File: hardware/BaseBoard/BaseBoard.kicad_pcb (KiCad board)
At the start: 2 copper layers, 81.3 x 106.7 mm, 83 parts, among them J1 I2C, J1-ESP1 ESP-1-L, J1-ESP2 ESP-1-L, J1-ESP3 ESP-1-L, J1-ESP4 ESP-1-L, J1-ESP5 ESP-1-L, J1-ESP6 ESP-1-L, J1-ESP7 ESP-1-L, J1-ESP8 ESP-1-L, J2 3V3P0_7, J2-ESP1 ESP-1-R, J2-ESP2 ESP-1-R, J2-ESP3 ESP-1-R, J2-ESP4 ESP-1-R, J2-ESP5 ESP-1-R, J2-ESP6 ESP-1-R, J2-ESP7 ESP-1-R, J2-ESP8 ESP-1-R, J3-BUS1 BUS-IN, J3-BUS2 BUS-IN, J3-BUS3 BUS-IN, J3-BUS4 BUS-IN, J3-BUS5 BUS-IN, J3-BUS6 BUS-IN, J3-BUS7 BUS-IN, J3-BUS8 BUS-IN, J4-BUS1 BUS-OUT, J4-BUS2 BUS-OUT, J4-BUS3 BUS-OUT, J4-BUS4 BUS-OUT, J4-BUS5 BUS-OUT, J4-BUS6 BUS-OUT, J4-BUS7 BUS-OUT, J4-BUS8 BUS-OUT, Q11 2N3904, Q12 AO3401A, Q21 2N3904, Q22 AO3401A, Q31 2N3904, Q32 AO3401A, Q41 2N3904, Q42 AO3401A, Q51 2N3904, Q52 AO3401A, Q61 2N3904, Q62 AO3401A, Q71 2N3904, Q72 AO3401A, Q81 2N3904, Q82 AO3401A, U1 AMS1117-3.3

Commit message: BaseBoard v1.1 update.
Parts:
- removed J1: I2C, Connector_PinSocket_2.54mm:PinSocket_1x04_P2.54mm_Vertical
- removed J2: 3V3P0_7, Connector_PinSocket_2.54mm:PinSocket_1x09_P2.54mm_Vertical
- added IC1: PCF8574RGTR, LIB_PCF8574RGTR:QFN50P300X300X100-17N-D, F.Cu at (179.4, 68.5)
- added R1: 10k, Resistor_SMD:R_0201_0603Metric, F.Cu at (180.6, 72.1)
- added R2: 10k, Resistor_SMD:R_0201_0603Metric, F.Cu at (181.9, 72.1)
- added R3: 10k, Resistor_SMD:R_0201_0603Metric, F.Cu at (179.3, 72.1)
- added R4: 10k, Resistor_SMD:R_0201_0603Metric, F.Cu at (181.2, 65.7)
- added R5: 10k, Resistor_SMD:R_0201_0603Metric, F.Cu at (182.2, 65.7)
- added R6: 10k, Resistor_SMD:R_0201_0603Metric, F.Cu at (183.3, 65.7)
- added SW1: SW_DIP_SPSTx03, Button_Switch_SMD:SW_DIP_SPSTx03_Slide_6.7x9.18mm_W8.61mm_P2.54mm_LowProfile, F.Cu at (189.5, 69.8)
- C1, C2: footprint Capacitor_THT:CP_Radial_D6.3mm_P2.50mm -> Capacitor_SMD:CP_Elec_4x5.3
- R11, R12, R21, R22, R31, R32, R41, R42, R51, R52, R61, R62, R71, R72, R81, R82: footprint Resistor_THT:R_Axial_DIN0207_L6.3mm_D2.5mm_P7.62mm_Horizontal -> Resistor_SMD:R_0603_1608Metric
- moved R22 12.0 mm to (177.8, 100.6), turned to -90 degrees
- moved R12 12.0 mm to (198.1, 100.6), turned to -90 degrees
- moved R32 12.0 mm to (157.5, 100.6), turned to -90 degrees
- moved R42 12.0 mm to (137.2, 100.6), turned to -90 degrees
- moved R62 11.5 mm to (147.3, 43.7), turned to 90 degrees
- moved R72 11.5 mm to (167.6, 43.7), turned to 90 degrees
- moved R52 11.5 mm to (127.0, 43.7), turned to 90 degrees
- moved R82 11.5 mm to (188.0, 43.7), turned to 90 degrees
- moved R51 9.74 mm to (133.3, 45.0), turned to 180 degrees
- moved R61 9.74 mm to (153.7, 45.0), turned to 180 degrees
- moved R81 9.74 mm to (194.3, 45.0), turned to 180 degrees
- moved R71 9.74 mm to (174.0, 45.0), turned to 180 degrees
- moved R11 9.23 mm to (191.8, 99.3), turned to 0 degrees
- moved R41 9.23 mm to (130.8, 99.3), turned to 0 degrees
- moved R21 9.23 mm to (171.4, 99.3), turned to 0 degrees
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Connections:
- net Net-(J1-Pin_1) renamed +3V3
- J1-ESP1 pad 6: unconnected-(J1-ESP1-Pin_6-Pad6) -> Net-(J1-ESP1-Pin_6)
- J1-ESP2 pad 6: unconnected-(J1-ESP2-Pin_6-Pad6) -> Net-(J1-ESP2-Pin_6)
- J1-ESP3 pad 6: unconnected-(J1-ESP3-Pin_6-Pad6) -> Net-(J1-ESP3-Pin_6)
- J1-ESP4 pad 6: unconnected-(J1-ESP4-Pin_6-Pad6) -> Net-(J1-ESP4-Pin_6)
- J1-ESP5 pad 6: unconnected-(J1-ESP5-Pin_6-Pad6) -> Net-(J1-ESP5-Pin_6)
- J1-ESP6 pad 6: unconnected-(J1-ESP6-Pin_6-Pad6) -> Net-(J1-ESP6-Pin_6)
- J1-ESP7 pad 6: unconnected-(J1-ESP7-Pin_6-Pad6) -> Net-(J1-ESP7-Pin_6)
- J1-ESP8 pad 6: unconnected-(J1-ESP8-Pin_6-Pad6) -> Net-(J1-ESP8-Pin_6)
- J3-BUS1 pad 2: GNDREF -> Net-(J1-ESP1-Pin_6)
- J3-BUS2 pad 2: GNDREF -> Net-(J1-ESP2-Pin_6)
- J3-BUS3 pad 2: GNDREF -> Net-(J1-ESP3-Pin_6)
- J3-BUS4 pad 2: GNDREF -> Net-(J1-ESP4-Pin_6)
- J3-BUS5 pad 2: GNDREF -> Net-(J1-ESP5-Pin_6)
- J3-BUS6 pad 2: GNDREF -> Net-(J1-ESP6-Pin_6)
- J3-BUS7 pad 2: GNDREF -> Net-(J1-ESP7-Pin_6)
- J3-BUS8 pad 2: GNDREF -> Net-(J1-ESP8-Pin_6)
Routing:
- net SWPIN-ESP4: track 24.9 -> 72.8 mm, vias 0 -> 2
- net SWPIN-ESP3: track 6.66 -> 52.4 mm, vias 0 -> 2
- net SWPIN-ESP5: track 25.4 -> 67.9 mm, vias 0 -> 2
- net SWPIN-ESP8: track 66.9 -> 34.6 mm, vias 0 -> 2
- net SWPIN-ESP2: track 14.3 -> 38.7 mm, vias 0 -> 2
- net SWPIN-ESP6: track 24.7 -> 47.9 mm, vias 0 -> 2
- net +3V3: track 17.6 -> 38.8 mm
- net SWPIN-ESP7: track 45.5 -> 27.8 mm, vias 0 -> 2
- net Net-(Q42-S): track 29.1 -> 13.9 mm
- net Net-(Q32-S): track 29.1 -> 13.9 mm
- net Net-(Q12-S): track 29.1 -> 13.9 mm
- net Net-(Q22-S): track 29.1 -> 13.9 mm
- net Net-(Q82-S): track 29.1 -> 14.0 mm
- net Net-(Q72-S): track 29.1 -> 14.0 mm
- net Net-(Q52-S): track 29.1 -> 14.4 mm
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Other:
- board text added: "COMChallange Baseboard v1.1 - github.com/raphweb"
- board text removed: "COMChallange Baseboard v1.0 - github.com/raphweb"

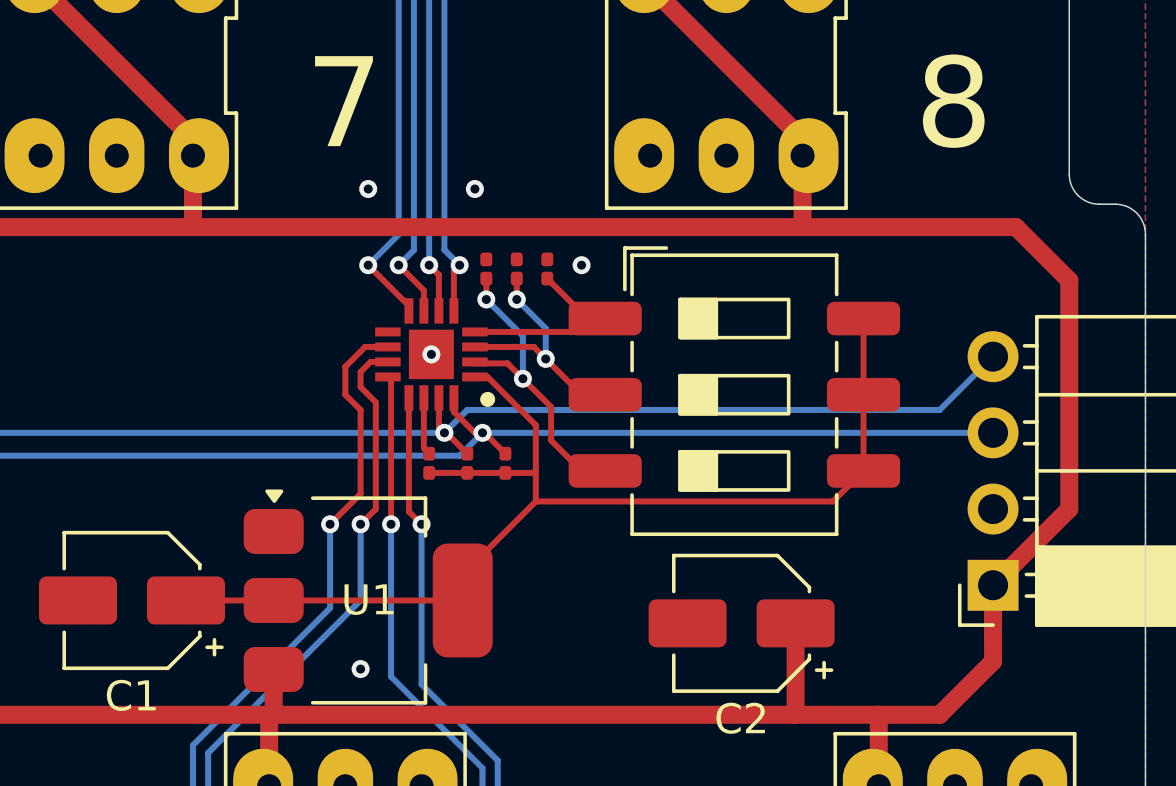
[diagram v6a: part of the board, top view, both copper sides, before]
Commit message: Enlarged smallest SMD resistors.
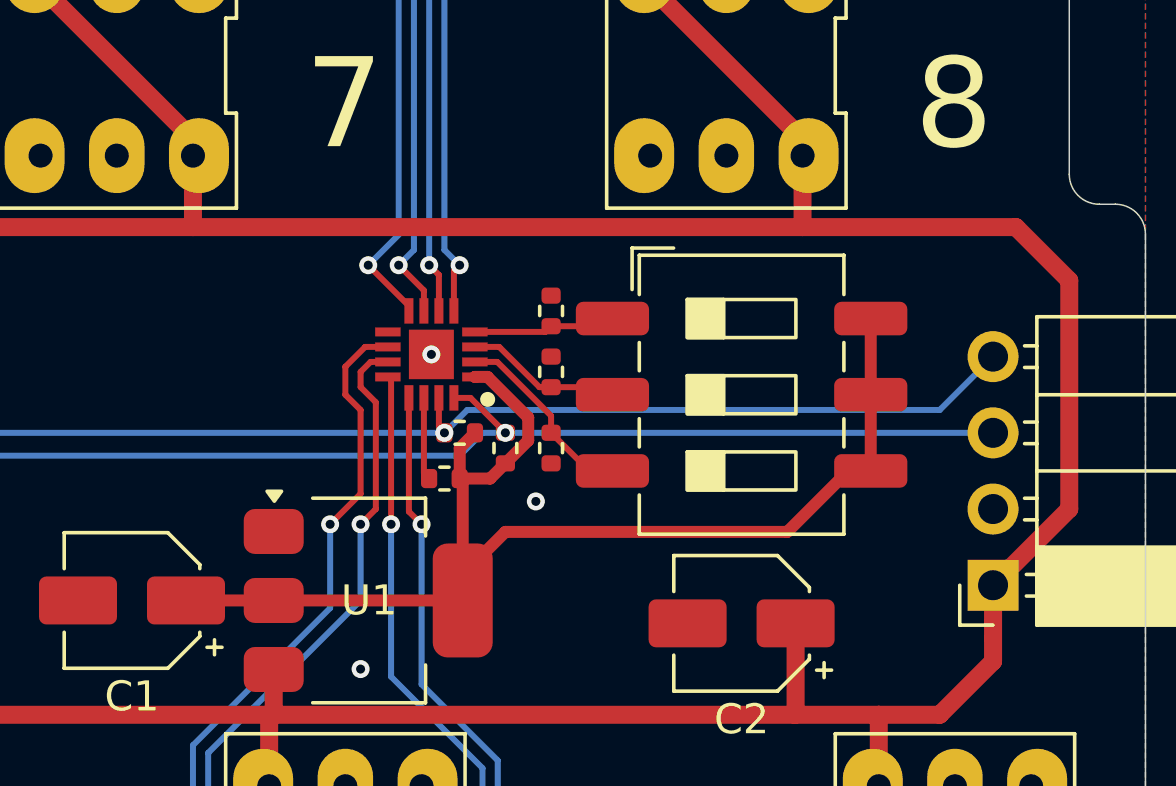
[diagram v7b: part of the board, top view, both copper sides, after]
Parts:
- R1, R2, R3, R4, R5, R6: footprint Resistor_SMD:R_0201_0603Metric -> Resistor_SMD:R_0402_1005Metric
- moved R4 6.35 mm to (183.4, 71.6), turned to -90 degrees
- moved R5 3.61 mm to (183.4, 69.1)
- moved R6 1.40 mm to (183.4, 67.1)
- moved R1 1.05 mm to (180.3, 71.1), turned to 0 degrees
- moved R3 0.72 mm to (179.8, 72.6), turned to 0 degrees
- moved R2 0.51 mm to (181.9, 71.6)
- moved SW1 0.24 mm to (189.7, 69.8)
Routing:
- net ADDR0: track 10.4 -> 6.42 mm, vias 2 -> 0
- net +3V3: track 38.8 -> 42.0 mm
- net ADDR1: track 8.08 -> 5.25 mm, vias 2 -> 0
- net ADDR2: track 7.01 -> 4.77 mm
- net I2C_SCL: track 75.5 -> 74.5 mm
- net INT: track 1.93 -> 2.76 mm
- net I2C_SDA: track 74.5 -> 73.9 mm
- net GNDREF: vias 25 -> 23

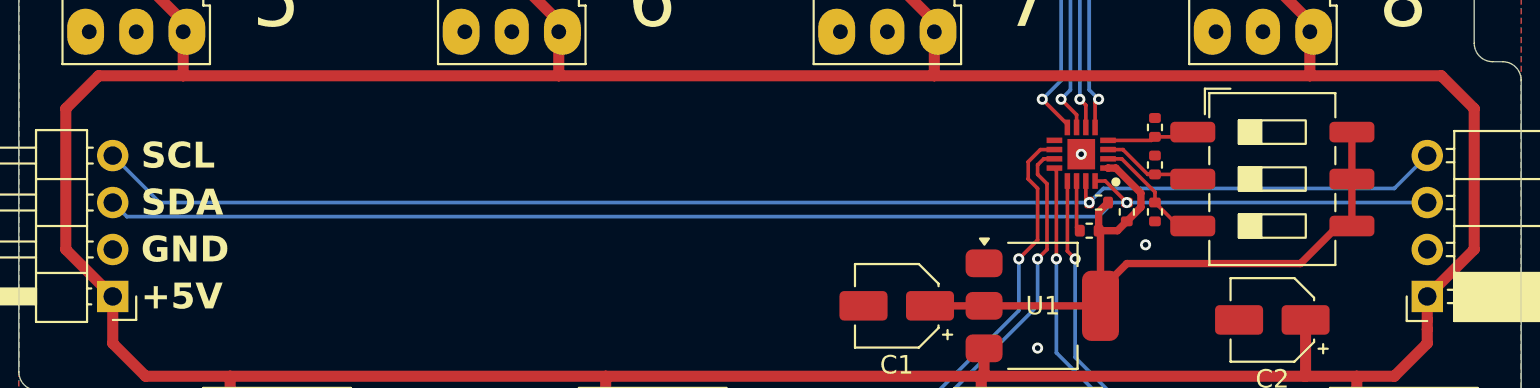
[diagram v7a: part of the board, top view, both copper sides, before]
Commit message: Fixed vias in small pads.
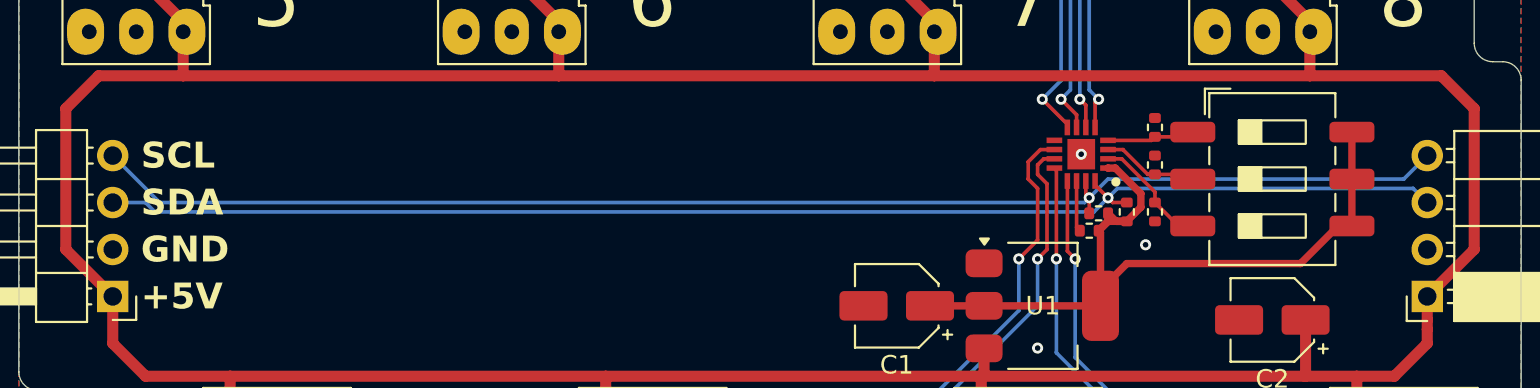
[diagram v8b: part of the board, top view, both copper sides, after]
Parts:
- moved R1 0.58 mm to (180.3, 71.7)
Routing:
- net +3V3: track 42.0 -> 42.6 mm
- net I2C_SDA: track 73.9 -> 74.5 mm
- net I2C_SCL: track 74.5 -> 75.0 mm
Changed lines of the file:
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@@
 	(footprint "Resistor_SMD:R_0402_1005Metric"
 		(layer "F.Cu")
-		(at 180.34 71.12)
+		(at 180.34 71.7042)
 		(descr "Resistor SMD 0402 (1005 Metric), square (rectangular) end terminal, IPC-7351 nominal, (Body size source: IPC-SM-782 page 72, https://www.pcb-3d.com/wordpress/wp-content/uploads/ipc-sm-782a_amendment_1_and_2.pdf), generated with kicad-footprint-generator")
 		(tags "resistor")
@@
 	)
 	(via
+		(at 179.398 68.506)
+		(size 0.6)
+		(drill 0.3)
+		(layers "F.Cu" "B.Cu")
+		(net 3)
+	)
+	(via
 		(at 174.244 86.614)
 		(size 0.6)
@@
 	)
 	(via
-		(at 179.398 68.506)
-		(size 0.6)
-		(drill 0.3)
-		(layers "F.Cu" "B.Cu")
-		(net 3)
-	)
-	(via
 		(at 195.58 34.29)
 		(size 4)
@@
 	)
 	(segment
-		(start 181.358 72.644)
-		(end 181.864 72.138)
+		(start 193.294 72.39)
+		(end 194.043 72.39)
 		(width 0.4)
 		(layer "F.Cu")
@@
 	)
 	(segment
-		(start 193.294 72.39)
-		(end 194.043 72.39)
+		(start 182.626 71.374)
+		(end 182.626 70.636636)
 		(width 0.4)
 		(layer "F.Cu")
@@
 	)
 	(segment
+		(start 181.864 72.138)
+		(end 181.864 72.136)
+		(width 0.4)
+		(layer "F.Cu")
+		(net 27)
+	)
+	(segment
+		(start 182.626 70.636636)
+		(end 181.245364 69.256)
+		(width 0.4)
+		(layer "F.Cu")
+		(net 27)
+	)
+	(segment
 		(start 180.442 76.708)
 		(end 180.442 75.844)
@@
 	)
 	(segment
+		(start 180.85 72.136)
+		(end 180.85 71.7042)
+		(width 0.4)
+		(layer "F.Cu")
+		(net 27)
+	)
+	(segment
+		(start 180.342 72.644)
+		(end 180.85 72.136)
+		(width 0.4)
+		(layer "F.Cu")
+		(net 27)
+	)
+	(segment
 		(start 194.043 72.39)
 		(end 194.043 69.85)
@@
 	)
 	(segment
-		(start 180.342 71.628)
-		(end 180.342 72.644)
+		(start 180.85 71.7042)
+		(end 181.2838 72.138)
 		(width 0.4)
 		(layer "F.Cu")
@@
 	)
 	(segment
-		(start 180.85 71.12)
-		(end 180.342 71.628)
+		(start 181.245364 69.256)
+		(end 180.848 69.256)
 		(width 0.4)
 		(layer "F.Cu")
@@
 	)
 	(segment
-		(start 180.342 72.644)
-		(end 181.358 72.644)
-		(width 0.4)
-		(layer "F.Cu")
-		(net 27)
-	)
-	(segment
 		(start 180.442 72.744)
 		(end 180.342 72.644)
@@
 	)
 	(segment
-		(start 174.142 76.708)
-		(end 180.442 76.708)
+		(start 181.2838 72.138)
+		(end 181.864 72.138)
 		(width 0.4)
 		(layer "F.Cu")
@@
 	)
 	(segment
-		(start 181.864 72.138)
-		(end 182.626 71.376)
+		(start 180.848 72.138)
+		(end 181.864 72.138)
 		(width 0.4)
 		(layer "F.Cu")
@@
 	)
 	(segment
-		(start 194.043 69.85)
-		(end 194.043 67.31)
+		(start 174.142 76.708)
+		(end 180.442 76.708)
 		(width 0.4)
 		(layer "F.Cu")
@@
 	)
 	(segment
-		(start 181.27 69.256)
-		(end 180.848 69.256)
+		(start 181.864 72.136)
+		(end 182.626 71.374)
 		(width 0.4)
 		(layer "F.Cu")
@@
 	)
 	(segment
-		(start 180.442 76.708)
-		(end 180.442 72.744)
+		(start 194.043 69.85)
+		(end 194.043 67.31)
 		(width 0.4)
 		(layer "F.Cu")
@@
 	)
 	(segment
-		(start 182.626 71.376)
-		(end 182.626 70.612)
+		(start 180.442 76.708)
+		(end 180.442 72.744)
 		(width 0.4)
 		(layer "F.Cu")
@@
 	)
 	(segment
-		(start 182.626 70.612)
-		(end 181.27 69.256)
+		(start 180.342 72.644)
+		(end 180.848 72.138)
 		(width 0.4)
 		(layer "F.Cu")
@@
 	)
 	(segment
-		(start 180.702 69.956)
+		(start 180.148 70.166)
 		(end 180.148 69.956)
 		(width 0.2)
@@
 	)
 	(segment
-		(start 181.864 71.118)
-		(end 180.702 69.956)
+		(start 180.848 70.866)
+		(end 180.148 70.166)
+		(width 0.2)
+		(layer "F.Cu")
+		(net 30)
+	)
+	(segment
+		(start 180.848 70.866)
+		(end 181.1 71.118)
+		(width 0.2)
+		(layer "F.Cu")
+		(net 30)
+	)
+	(segment
+		(start 181.1 71.118)
+		(end 181.864 71.118)
 		(width 0.2)
 		(layer "F.Cu")
@@
 	)
 	(via
-		(at 181.864 71.12)
+		(at 180.848 70.866)
 		(size 0.6)
 		(drill 0.3)
@@
 	)
 	(segment
-		(start 181.102 71.12)
-		(end 180.34 71.882)
+		(start 180.086 71.628)
+		(end 129.286 71.628)
 		(width 0.2)
 		(layer "B.Cu")
@@
 	)
 	(segment
-		(start 198.12 71.12)
-		(end 181.864 71.12)
+		(start 128.778 71.12)
+		(end 127 71.12)
 		(width 0.2)
 		(layer "B.Cu")
@@
 	)
 	(segment
-		(start 127.762 71.882)
-		(end 127 71.12)
+		(start 197.358 70.358)
+		(end 198.12 71.12)
 		(width 0.2)
 		(layer "B.Cu")
@@
 	)
 	(segment
-		(start 181.864 71.12)
-		(end 181.102 71.12)
+		(start 180.848 70.866)
+		(end 180.086 71.628)
 		(width 0.2)
 		(layer "B.Cu")
@@
 	)
 	(segment
-		(start 180.34 71.882)
-		(end 127.762 71.882)
+		(start 180.848 70.866)
+		(end 181.356 70.358)
 		(width 0.2)
 		(layer "B.Cu")
@@
 	)
 	(segment
-		(start 179.898 71.12)
-		(end 179.832 71.12)
+		(start 129.286 71.628)
+		(end 128.778 71.12)
+		(width 0.2)
+		(layer "B.Cu")
+		(net 30)
+	)
+	(segment
+		(start 181.356 70.358)
+		(end 197.358 70.358)
+		(width 0.2)
+		(layer "B.Cu")
+		(net 30)
+	)
+	(segment
+		(start 179.648 69.956)
+		(end 179.648 70.682)
 		(width 0.2)
 		(layer "F.Cu")
@@
 	)
 	(segment
-		(start 179.648 70.936)
-		(end 179.648 69.956)
+		(start 179.832 71.7022)
+		(end 179.83 71.7042)
 		(width 0.2)
 		(layer "F.Cu")
@@
 	)
 	(segment
-		(start 179.832 71.12)
-		(end 179.648 70.936)
+		(start 179.648 70.682)
+		(end 179.832 70.866)
+		(width 0.2)
+		(layer "F.Cu")
+		(net 31)
+	)
+	(segment
+		(start 179.832 70.866)
+		(end 179.832 71.7022)
 		(width 0.2)
 		(layer "F.Cu")
@@
 	)
 	(via
-		(at 179.832 71.12)
+		(at 179.832 70.866)
 		(size 0.6)
 		(drill 0.3)
@@
 	)
 	(segment
-		(start 180.594 70.358)
-		(end 179.832 71.12)
+		(start 179.832 70.866)
+		(end 179.578 71.12)
 		(width 0.2)
 		(layer "B.Cu")
@@
 	)
 	(segment
-		(start 196.342 70.358)
-		(end 182.626 70.358)
+		(start 179.832 70.866)
+		(end 180.848 69.85)
 		(width 0.2)
 		(layer "B.Cu")
@@
 	(segment
 		(start 129.54 71.12)
-		(end 179.832 71.12)
+		(end 127 68.58)
 		(width 0.2)
 		(layer "B.Cu")
@@
 	)
 	(segment
-		(start 127 68.58)
-		(end 129.54 71.12)
+		(start 180.848 69.85)
+		(end 196.85 69.85)
 		(width 0.2)
 		(layer "B.Cu")
@@
 	)
 	(segment
-		(start 198.12 68.58)
-		(end 196.342 70.358)
+		(start 179.578 71.12)
+		(end 129.54 71.12)
 		(width 0.2)
 		(layer "B.Cu")
@@
 	)
 	(segment
-		(start 182.626 70.358)
-		(end 180.594 70.358)
+		(start 196.85 69.85)
+		(end 198.12 68.58)
 		(width 0.2)
 		(layer "B.Cu")
